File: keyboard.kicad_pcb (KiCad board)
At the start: 2 copper layers, 168.3 x 124.5 mm, 135 parts, among them J1 Conn_01x06_Socket, J2 Conn_01x02_Socket, J3 Conn_01x02_Socket, J4 Conn_01x06_Socket, SW1 SW_Push, SW10 SW_Push, SW11 SW_Push, SW12 SW_Push, SW13 SW_Push, SW14 SW_Push, SW15 SW_Push, SW16 SW_Push, SW17 SW_Push, SW18 SW_Push, SW19 SW_Push, SW2 SW_Push, SW20 SW_Push, SW21 SW_Push, SW22 SW_Push, SW23 SW_Push, SW24 SW_Push, SW25 SW_Push, SW26 SW_Push, SW27 SW_Push, SW28 SW_Push, SW29 SW_Push, SW3 SW_Push, SW30 SW_Push, SW31 SW_Push, SW32 SW_Push, SW33 SW_Push, SW34 SW_Push, SW35 SW_Push, SW36 SW_Push, SW37 SW_Push, SW38 SW_Push, SW39 SW_Push, SW4 SW_Push, SW40 SW_Push, SW41 SW_Push, SW42 SW_Push, SW43 SW_Push, SW44 SW_Push, SW45 SW_Push, SW46 SW_Push, SW47 SW_Push, SW48 SW_Push, SW49 SW_Push, SW5 SW_Push, SW50 SW_Push, SW51 SW_Push, SW52 SW_Push, SW53 SW_Push, SW54 SW_Push, SW55 SW_Push, SW56 SW_Push, SW57 SW_Push, SW58 SW_Push, SW59 SW_Push, SW6 SW_Push, SW60 SW_Push, SW7 SW_Push, SW8 SW_Push, SW9 SW_Push, U1 rp2040-zero

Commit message: 実は耐えてた
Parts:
- added U2: rp2040-zero, mcu:rp2040-zero-smd_reverse_flush_B, B.Cu at (192.4, 55.6)
- U1: footprint mcu:rp2040-zero-tht -> mcu:rp2040-zero-smd_reverse_flush_A; moved to F.Cu
- moved U1 1.42 mm to (192.4, 55.6), turned to 0 degrees

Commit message: 抵抗の配置を直したのでcommit
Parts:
- removed J3: Conn_01x02_Socket, Connector_PinHeader_2.54mm:PinHeader_1x02_P2.54mm_Vertical
- removed J4: Conn_01x06_Socket, Connector_PinHeader_2.54mm:PinHeader_1x06_P2.54mm_Vertical
- removed JP1, JP2: Jumper_2_Open, Jumper:SolderJumper-2_P1.3mm_Open_Pad1.0x1.5mm
- removed R5, R6: R, Resistor_SMD:R_1206_3216Metric_Pad1.30x1.75mm_HandSolder
- J1: value Conn_01x06_Socket -> Conn_01x09_Socket; footprint Connector_PinHeader_2.54mm:PinHeader_1x06_P2.54mm_Vertical -> Connector_PinSocket_2.54mm:PinSocket_1x09_P2.54mm_Vertical
- J2: value Conn_01x02_Socket -> Conn_01x09_Socket; footprint Connector_PinHeader_2.54mm:PinHeader_1x02_P2.54mm_Vertical -> Connector_PinSocket_2.54mm:PinSocket_1x09_P2.54mm_Vertical
- JC1: footprint Connector_Audio:Jack_3.5mm_PJ320E_Horizontal -> kbd:MJ-4PP-9; moved to F.Cu
- JC2: footprint Connector_Audio:Jack_3.5mm_PJ320E_Horizontal -> kbd:MJ-4PP-9; moved to B.Cu
- R1, R2: moved to F.Cu
- R4: moved to B.Cu
- U1: footprint mcu:rp2040-zero-smd_reverse_flush_A -> mcu:rp2040-zero-smd_flush_front
- U2: footprint mcu:rp2040-zero-smd_reverse_flush_B -> mcu:rp2040-zero-smd_flush_back
- moved JC1 25.1 mm to (202.3, 74.2), turned to -90 degrees
- moved J1 16.6 mm to (194.8, 81.9)
- moved J2 7.24 mm to (192.1, 81.9)
- moved R3 5.16 mm to (185.2, 71.7)
- moved R4 4.97 mm to (185.2, 75.2), turned to 180 degrees
- moved JC2 4.79 mm to (202.3, 72.2), turned to 90 degrees
- moved D20 1.85 mm to (189.9, 142.6)
- moved R2 1.67 mm to (185.2, 75.2), turned to 0 degrees
- moved R1 1.43 mm to (185.2, 71.7), turned to 0 degrees
- moved D28 0.65 mm to (171.9, 106.1)
- moved D59 0.62 mm to (171.9, 108.6)
- moved D42 0.50 mm to (114.6, 63.5)
- moved D50 0.49 mm to (195.7, 120.7)
- moved D51 0.48 mm to (152.7, 48.2)
- moved D26 0.43 mm to (171.9, 68.0)
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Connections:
- D31 pad 1: l_row0 -> r_row0
- D32 pad 1: l_row1 -> r_row1
- D33 pad 1: l_row2 -> r_row2
- D34 pad 1: l_row3 -> r_row3
- D35 pad 1: l_row4 -> r_row4
- D36 pad 1: l_row0 -> r_row0
- D37 pad 1: l_row1 -> r_row1
- D38 pad 1: l_row2 -> r_row2
- D39 pad 1: l_row3 -> r_row3
- D40 pad 1: l_row4 -> r_row4
- D41 pad 1: l_row0 -> r_row0
- D42 pad 1: l_row1 -> r_row1
- D43 pad 1: l_row2 -> r_row2
- D44 pad 1: l_row3 -> r_row3
- D45 pad 1: l_row4 -> r_row4
- D46 pad 1: l_row0 -> r_row0
- D47 pad 1: l_row1 -> r_row1
- D48 pad 1: l_row2 -> r_row2
- D49 pad 1: l_row3 -> r_row3
- D50 pad 1: l_row4 -> r_row4
- D51 pad 1: l_row0 -> r_row0
- D52 pad 1: l_row1 -> r_row1
- D53 pad 1: l_row2 -> r_row2
- D54 pad 1: l_row3 -> r_row3
- D55 pad 1: l_row4 -> r_row4
- D56 pad 1: l_row0 -> r_row0
- D57 pad 1: l_row1 -> r_row1
- D58 pad 1: l_row2 -> r_row2
- D59 pad 1: l_row3 -> r_row3
- D60 pad 1: l_row4 -> r_row4
- R1 pad 1: Net-(J1-Pin_6) -> Net-(J2-Pin_6)
- R2 pad 1: Net-(J1-Pin_6) -> Net-(J2-Pin_6)
- R3 pad 1: Net-(JP1-B) -> Net-(J1-Pin_6)
- R3 pad 2: Net-(J1-Pin_5) -> Net-(U2-26)
- R4 pad 1: Net-(J4-Pin_6) -> Net-(J1-Pin_6)
- R4 pad 2: Net-(U2-26) -> Net-(U2-27)
- SW31 pad 1: l_col0 -> r_col0
- SW32 pad 1: l_col0 -> r_col0
- SW33 pad 1: l_col0 -> r_col0
- SW34 pad 1: l_col0 -> r_col0
- SW35 pad 1: l_col0 -> r_col0
- SW36 pad 1: l_col1 -> r_col1
- SW37 pad 1: l_col1 -> r_col1
- SW38 pad 1: l_col1 -> r_col1
- SW39 pad 1: l_col1 -> r_col1
- SW40 pad 1: l_col1 -> r_col1
- SW41 pad 1: l_col2 -> r_col2
- SW42 pad 1: l_col2 -> r_col2
- SW43 pad 1: l_col2 -> r_col2
- SW44 pad 1: l_col2 -> r_col2
- SW45 pad 1: l_col2 -> r_col2
- SW46 pad 1: l_col3 -> r_col3
- SW47 pad 1: l_col3 -> r_col3
- SW48 pad 1: l_col3 -> r_col3
- SW49 pad 1: l_col3 -> r_col3
- SW50 pad 1: l_col3 -> r_col3
- SW51 pad 1: l_col4 -> r_col4
- SW52 pad 1: l_col4 -> r_col4
- SW53 pad 1: l_col4 -> r_col4
- SW54 pad 1: l_col4 -> r_col4
- SW55 pad 1: l_col4 -> r_col4
- SW56 pad 1: l_col5 -> r_col5
- SW57 pad 1: l_col5 -> r_col5
- SW58 pad 1: l_col5 -> r_col5
- SW59 pad 1: l_col5 -> r_col5
- SW60 pad 1: l_col5 -> r_col5
- U1 pad 1: Net-(J1-Pin_1) -> Net-(J2-Pin_1)
- U1 pad 16: Net-(J1-Pin_5) -> l_row4
- U1 pad 19: Net-(J3-Pin_2) -> Net-(J2-Pin_8)
- U1 pad 2: Net-(J1-Pin_2) -> Net-(J2-Pin_2)
- U1 pad 20: Net-(J3-Pin_1) -> Net-(J2-Pin_9)
- U1 pad 22: Net-(J1-Pin_5) -> Net-(J2-Pin_5)
- U1 pad 23: Net-(J1-Pin_6) -> Net-(J2-Pin_6)
- U1 pad 3: Net-(J1-Pin_3) -> Net-(J2-Pin_3)
- U1 pad 4: Net-(J1-Pin_4) -> Net-(J2-Pin_4)
- U2 pad 1: Net-(J4-Pin_1) -> Net-(J1-Pin_1)
- U2 pad 10: l_col5 -> r_col5
- U2 pad 11: l_row0 -> r_row0
- U2 pad 12: l_row1 -> r_row1
- U2 pad 13: l_row2 -> r_row2
- U2 pad 14: l_row3 -> r_row3
- U2 pad 15: l_row4 -> r_row4
- U2 pad 16: Net-(J4-Pin_5) -> r_row4
- U2 pad 19: Net-(J2-Pin_2) -> Net-(J1-Pin_8)
- U2 pad 2: Net-(J4-Pin_2) -> Net-(J1-Pin_2)
- U2 pad 20: Net-(J2-Pin_1) -> Net-(J1-Pin_9)
- U2 pad 22: Net-(J4-Pin_5) -> Net-(J1-Pin_5)
- U2 pad 23: Net-(J4-Pin_6) -> Net-(J1-Pin_6)
- U2 pad 3: Net-(J4-Pin_3) -> Net-(J1-Pin_3)
- U2 pad 4: Net-(J4-Pin_4) -> Net-(J1-Pin_4)
- U2 pad 5: l_col0 -> r_col0
- U2 pad 6: l_col1 -> r_col1
- U2 pad 7: l_col2 -> r_col2
- U2 pad 8: l_col3 -> r_col3
- U2 pad 9: l_col4 -> r_col4
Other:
- outline, holes or cut-outs redrawn

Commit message: とりまcommit
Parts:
- moved J2 90.4 mm to (128.0, 145.5), turned to 0 degrees
- moved J1 20.6 mm to (192.4, 102.4), turned to 180 degrees
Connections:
- J1 pad 7: r_row4 -> Net-(J1-Pin_7)
- J2 pad 7: l_row4 -> Net-(J2-Pin_7)
- U1 pad 16: l_row4 -> Net-(J2-Pin_7)
- U2 pad 16: r_row4 -> Net-(J1-Pin_7)

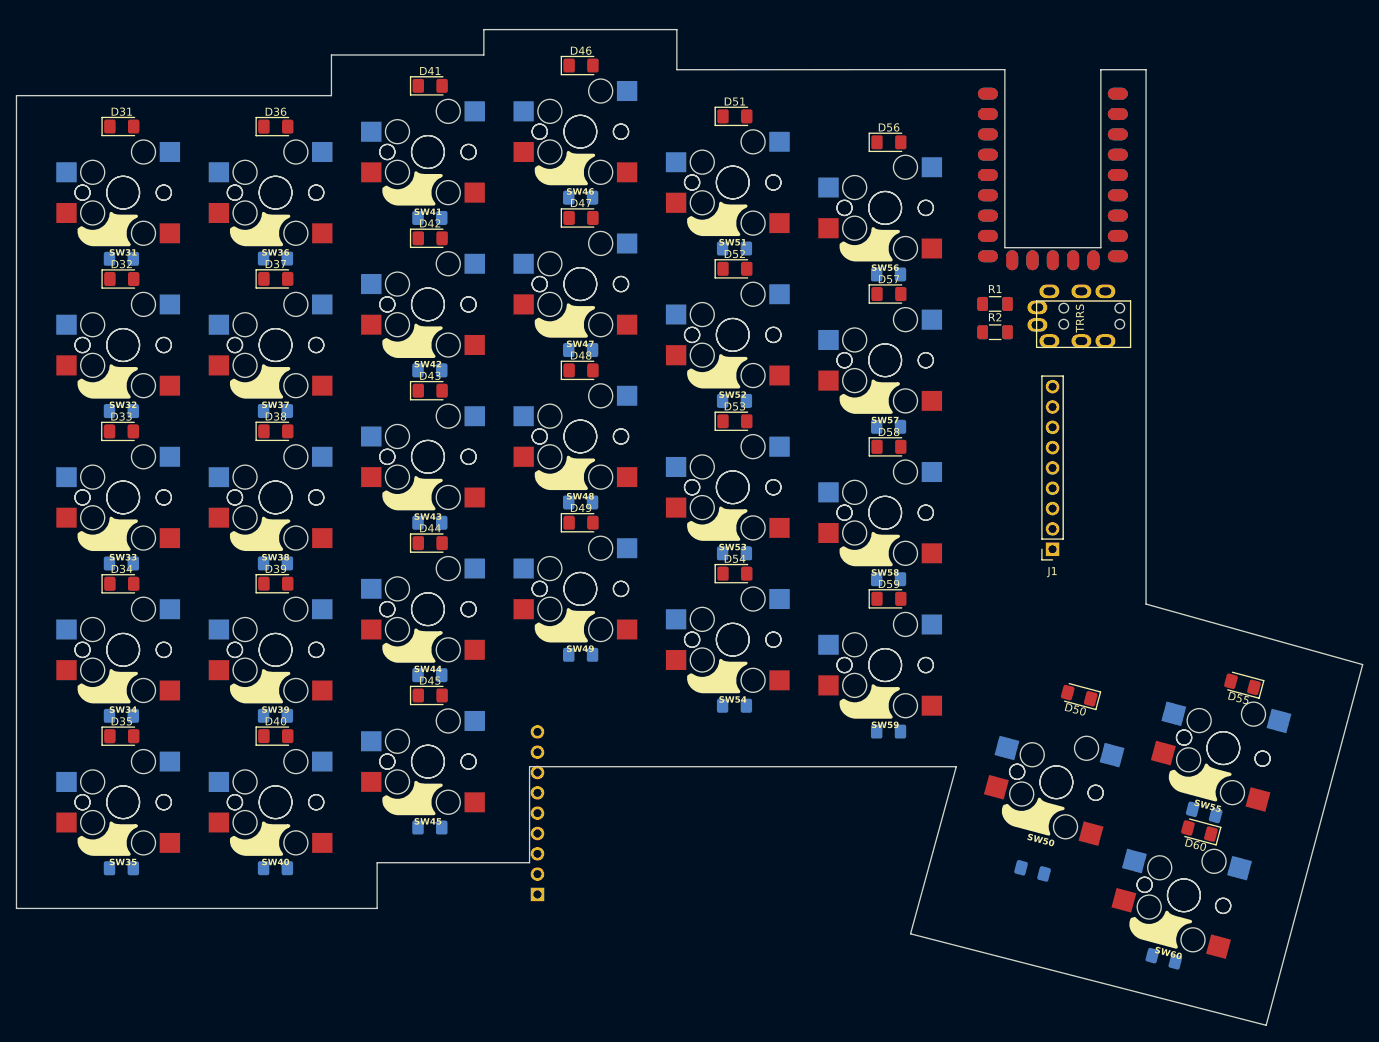
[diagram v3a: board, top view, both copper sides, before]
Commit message: 基板外形完成
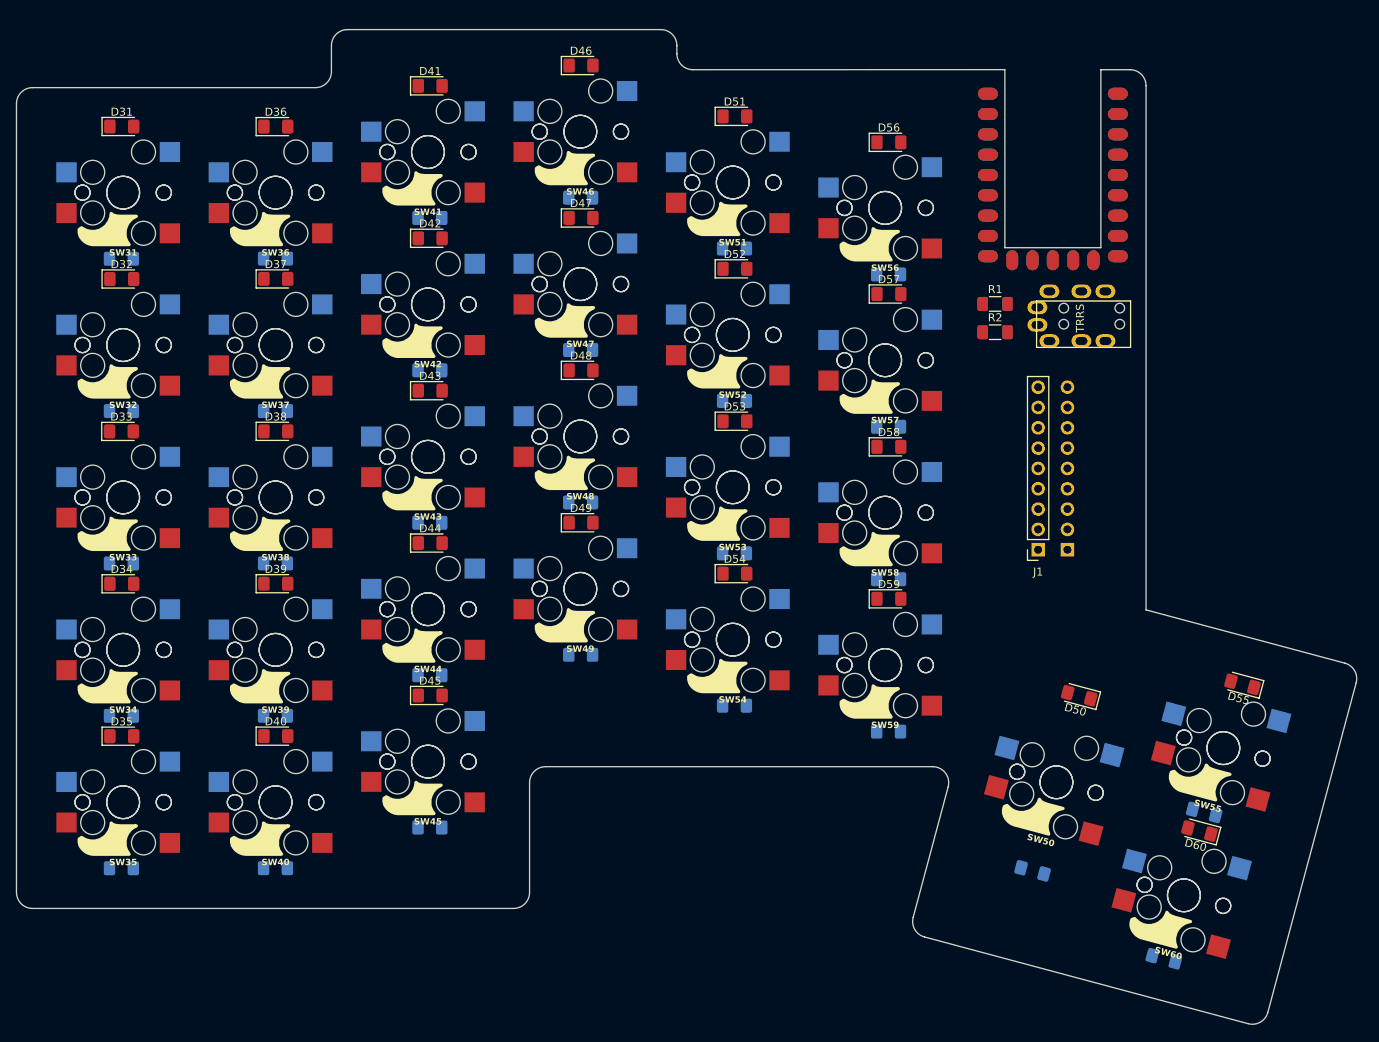
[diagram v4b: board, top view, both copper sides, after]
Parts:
- moved J2 79.0 mm to (194.2, 102.4)
- moved J1 1.81 mm to (190.6, 102.4)
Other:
- board size 168.3 x 124.5 mm -> 167.5 x 124.3 mm
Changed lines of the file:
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@@
 	(footprint "Connector_PinSocket_2.54mm:PinSocket_1x09_P2.54mm_Vertical"
 		(layer "F.Cu")
-		(at 192.375 102.36 180)
+		(at 190.57 102.42 180)
 		(descr "Through hole straight socket strip, 1x09, 2.54mm pitch, single row (from Kicad 4.0.7), script generated")
 		(tags "Through hole socket strip THT 1x09 2.54mm single row")
@@
 		)
 		(fp_text user "${REFERENCE}"
-			(at 0 10.16 270)
+			(at 0 10.16 -90)
 			(layer "F.Fab")
 			(effects
@@
 	(footprint "Connector_PinSocket_2.54mm:PinSocket_1x09_P2.54mm_Vertical"
 		(layer "B.Cu")
-		(at 127.99 145.51)
+		(at 194.235 102.42)
 		(descr "Through hole straight socket strip, 1x09, 2.54mm pitch, single row (from Kicad 4.0.7), script generated")
 		(tags "Through hole socket strip THT 1x09 2.54mm single row")
 		(property "Reference" "J2"
-			(at 0 2.77 360)
+			(at 0 2.77 0)
 			(layer "B.SilkS")
 			(effects
@@
 		)
 		(property "Value" "Conn_01x09_Socket"
-			(at 0 -23.09 360)
+			(at 0 -23.09 0)
 			(layer "B.Fab")
 			(effects
@@
 	)
 	(gr_line
-		(start 62.865 45.659)
-		(end 102.235 45.659)
+		(start 64.865 44.659)
+		(end 100.235 44.659)
+		(stroke
+			(width 0.12)
+			(type default)
+		)
+		(layer "Edge.Cuts")
+	)
+	(gr_arc
+		(start 102.235 39.404)
+		(mid 102.820786 37.989786)
+		(end 104.235 37.404)
 		(stroke
 			(width 0.12)
@@
 	)
 	(gr_line
-		(start 102.235 45.659)
-		(end 102.235 40.579)
+		(start 102.235 42.659)
+		(end 102.235 39.404)
 		(stroke
 			(width 0.12)
@@
 	(gr_line
 		(start 186.41 42.41)
-		(end 145.415 42.418)
+		(end 147.41539 42.41761)
 		(stroke
 			(width 0.12)
@@
 	)
 	(gr_line
-		(start 180.34 129.54)
-		(end 174.625 150.434)
+		(start 174.953029 148.375553)
+		(end 179.325401 132.057638)
 		(stroke
 			(width 0.12)
@@
 		(layer "Edge.Cuts")
 	)
-	(gr_line
-		(start 121.285 40.579)
-		(end 121.285 37.404)
+	(gr_arc
+		(start 228.912158 116.598474)
+		(mid 230.126605 117.530317)
+		(end 230.326417 119.047976)
 		(stroke
 			(width 0.12)
@@
 		(layer "Edge.Cuts")
 	)
-	(gr_line
-		(start 121.285 40.579)
-		(end 102.235 40.579)
+	(gr_arc
+		(start 127 131.54)
+		(mid 127.585786 130.125786)
+		(end 129 129.54)
 		(stroke
 			(width 0.12)
@@
 	)
 	(gr_line
-		(start 107.95 141.544)
-		(end 127 141.544)
+		(start 127 145.259)
+		(end 127 131.54)
 		(stroke
 			(width 0.12)
@@
 		(layer "Edge.Cuts")
 	)
-	(gr_line
-		(start 127 141.544)
-		(end 127 129.54)
+	(gr_arc
+		(start 177.393549 129.54)
+		(mid 178.980218 130.322491)
+		(end 179.325401 132.057638)
 		(stroke
 			(width 0.12)
@@
 	)
 	(gr_line
-		(start 107.95 147.259)
-		(end 107.95 141.544)
+		(start 176.367243 150.825043)
+		(end 216.835719 161.668539)
 		(stroke
 			(width 0.12)
@@
 	)
 	(gr_line
-		(start 174.625 150.434)
-		(end 219.075 161.864)
+		(start 104.235 37.404)
+		(end 143.415 37.404)
 		(stroke
 			(width 0.12)
@@
 		(layer "Edge.Cuts")
 	)
-	(gr_line
-		(start 121.285 37.404)
-		(end 145.415 37.404)
+	(gr_arc
+		(start 102.235 42.659)
+		(mid 101.649214 44.073214)
+		(end 100.235 44.659)
+		(stroke
+			(width 0.12)
+			(type default)
+		)
+		(layer "Edge.Cuts")
+	)
+	(gr_arc
+		(start 143.415 37.404)
+		(mid 144.829214 37.989786)
+		(end 145.415 39.404)
 		(stroke
 			(width 0.12)
@@
 	)
 	(gr_line
-		(start 62.865 45.659)
-		(end 62.865 147.259)
+		(start 62.865 46.659)
+		(end 62.865 145.259)
 		(stroke
 			(width 0.12)
@@
 	)
 	(gr_line
-		(start 204.06 109.22)
-		(end 204.06 42.418)
+		(start 204.06 109.94)
+		(end 204.06 44.418)
 		(stroke
 			(width 0.12)
@@
 	)
 	(gr_line
-		(start 204.06 42.418)
+		(start 202.06 42.418)
 		(end 198.41 42.418)
 		(stroke
@@
 		(layer "Edge.Cuts")
 	)
+	(gr_arc
+		(start 176.367243 150.825043)
+		(mid 175.152846 149.893188)
+		(end 174.953029 148.375553)
+		(stroke
+			(width 0.12)
+			(type default)
+		)
+		(layer "Edge.Cuts")
+	)
+	(gr_arc
+		(start 219.285209 160.254325)
+		(mid 218.353359 161.468723)
+		(end 216.835719 161.668539)
+		(stroke
+			(width 0.12)
+			(type default)
+		)
+		(layer "Edge.Cuts")
+	)
+	(gr_arc
+		(start 147.41539 42.41761)
+		(mid 146.000924 41.831961)
+		(end 145.415 40.41761)
+		(stroke
+			(width 0.12)
+			(type default)
+		)
+		(layer "Edge.Cuts")
+	)
+	(gr_arc
+		(start 202.06 42.418)
+		(mid 203.474214 43.003786)
+		(end 204.06 44.418)
+		(stroke
+			(width 0.12)
+			(type default)
+		)
+		(layer "Edge.Cuts")
+	)
 	(gr_line
-		(start 231.14 116.779)
-		(end 204.061409 109.214955)
+		(start 228.912158 116.598474)
+		(end 204.06 109.94)
+		(stroke
+			(width 0.12)
+			(type default)
+		)
+		(layer "Edge.Cuts")
+	)
+	(gr_arc
+		(start 127 145.259)
+		(mid 126.414214 146.673214)
+		(end 125 147.259)
 		(stroke
 			(width 0.12)
@@
 	)
 	(gr_line
-		(start 145.415 37.404)
-		(end 145.415 42.418)
+		(start 145.415 39.404)
+		(end 145.415 40.41761)
 		(stroke
 			(width 0.12)
@@
 	)
 	(gr_line
-		(start 62.865 147.259)
-		(end 107.95 147.259)
+		(start 64.865 147.259)
+		(end 125 147.259)
+		(stroke
+			(width 0.12)
+			(type default)
+		)
+		(layer "Edge.Cuts")
+	)
+	(gr_arc
+		(start 62.865 46.659)
+		(mid 63.450786 45.244786)
+		(end 64.865 44.659)
 		(stroke
 			(width 0.12)
@@
 	)
 	(gr_line
-		(start 219.075 161.864)
-		(end 231.14 116.779)
+		(start 219.285209 160.254325)
+		(end 230.326417 119.047976)
+		(stroke
+			(width 0.12)
+			(type default)
+		)
+		(layer "Edge.Cuts")
+	)
+	(gr_arc
+		(start 64.865 147.259)
+		(mid 63.450786 146.673214)
+		(end 62.865 145.259)
 		(stroke
 			(width 0.12)
@@
 	)
 	(gr_line
-		(start 127 129.54)
-		(end 180.34 129.54)
+		(start 129 129.54)
+		(end 177.393549 129.54)
 		(stroke
 			(width 0.12)

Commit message: ネジ穴を配置
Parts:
- added H1: MountingHole, MountingHole:MountingHole_2.2mm_M2, F.Cu at (65.4, 47.3)
- added H10: MountingHole, MountingHole:MountingHole_2.2mm_M2, F.Cu at (142.9, 39.9)
- added H11: MountingHole, MountingHole:MountingHole_2.2mm_M2, F.Cu at (201.5, 108.6)
- added H12: MountingHole, MountingHole:MountingHole_2.2mm_M2, F.Cu at (152.6, 127.0)
- added H2: MountingHole, MountingHole:MountingHole_2.2mm_M2, F.Cu at (65.5, 144.7)
- added H3: MountingHole, MountingHole:MountingHole_2.2mm_M2, F.Cu at (124.4, 144.7)
- added H4: MountingHole, MountingHole:MountingHole_2.2mm_M2, F.Cu at (178.3, 45.0)
- added H5: MountingHole, MountingHole:MountingHole_2.2mm_M2, F.Cu at (216.9, 159.0)
- added H6: MountingHole, MountingHole:MountingHole_2.2mm_M2, F.Cu at (227.7, 118.9)
- added H7: MountingHole, MountingHole:MountingHole_2.2mm_M2, F.Cu at (201.6, 81.6)
- added H8: MountingHole, MountingHole:MountingHole_2.2mm_M2, F.Cu at (177.6, 148.5)
- added H9: MountingHole, MountingHole:MountingHole_2.2mm_M2, F.Cu at (104.8, 40.0)
